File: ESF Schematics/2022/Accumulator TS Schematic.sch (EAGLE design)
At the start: 58 parts

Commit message: More schematic updates
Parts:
- removed U$10: CONNECTOR-2_HPK, HyTechSymbolsTemp:CONNECTOR-2_HPK
- added J1, J2: CONNECTOR-1_LCAX2-14F-E, HyTechSymbolsTemp:CONNECTOR-1_LCAX2-14F-E
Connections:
- net GND: now also U$11.GND
- net SHDN: now also U$11.VCC
- net TS+UNFUSED: now also J2.1; no longer U$10.1
- net TS-UNFUSED: now also J1.1; no longer U$10.2
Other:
- note added: "10 mil"
- note added: "10 mil:"
- note added: "16AWG"
- note added: "16AWG:"
- note added: "22AWG"
- note removed: "35mm^2:"
- moved on the sheet: F3

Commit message: final drafts of most schematics
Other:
- note added: "17.5mm^2:"
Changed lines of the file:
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@@
 <text x="12.7" y="53.34" size="3.048" layer="97" align="top-left">Wire Gauge Key</text>
 <text x="12.7" y="35.56" size="1.778" layer="97" align="top-left">22AWG:</text>
-<text x="12.7" y="45.72" size="1.778" layer="97" align="top-left">20mm^2</text>
+<text x="12.7" y="45.72" size="1.778" layer="97" align="top-left">17.5mm^2:</text>
 <wire x1="241.3" y1="101.6" x2="269.24" y2="101.6" width="0.1524" layer="97" style="shortdash"/>
 <wire x1="269.24" y1="101.6" x2="269.24" y2="86.36" width="0.1524" layer="97" style="shortdash"/>
@@
 <segment>
 <pinref part="U$6" gate="G$1" pin="-"/>
-<wire x1="129.54" y1="144.78" x2="134.62" y2="144.78" width="0.508" layer="91"/>
-<wire x1="134.62" y1="144.78" x2="134.62" y2="152.4" width="0.508" layer="91"/>
+<wire x1="129.54" y1="144.78" x2="134.62" y2="144.78" width="0.4445" layer="91"/>
+<wire x1="134.62" y1="144.78" x2="134.62" y2="152.4" width="0.4445" layer="91"/>
 <pinref part="U$15" gate="G$1" pin="2"/>
-<wire x1="139.7" y1="152.4" x2="134.62" y2="152.4" width="0.508" layer="91"/>
+<wire x1="139.7" y1="152.4" x2="134.62" y2="152.4" width="0.4445" layer="91"/>
 </segment>
 </net>
@@
 </segment>
 <segment>
-<wire x1="86.36" y1="154.94" x2="86.36" y2="172.72" width="0.508" layer="91"/>
+<wire x1="86.36" y1="154.94" x2="86.36" y2="172.72" width="0.4445" layer="91"/>
 <pinref part="U$3" gate="G$1" pin="+"/>
-<wire x1="86.36" y1="172.72" x2="91.44" y2="172.72" width="0.508" layer="91"/>
+<wire x1="86.36" y1="172.72" x2="91.44" y2="172.72" width="0.4445" layer="91"/>
 <label x="68.58" y="154.94" size="1.27" layer="95"/>
 <pinref part="U$16" gate="G$1" pin="1"/>
-<wire x1="78.74" y1="154.94" x2="86.36" y2="154.94" width="0.508" layer="91"/>
+<wire x1="78.74" y1="154.94" x2="86.36" y2="154.94" width="0.4445" layer="91"/>
 </segment>
 <segment>
@@
 <segment>
 <pinref part="AIR+" gate="G$1" pin="CONTACT1"/>
-<wire x1="53.34" y1="152.4" x2="48.26" y2="152.4" width="0.508" layer="91"/>
+<wire x1="53.34" y1="152.4" x2="48.26" y2="152.4" width="0.4445" layer="91"/>
 <pinref part="MAIN_FUSE" gate="G$1" pin="2"/>
 </segment>
@@
 <segment>
 <pinref part="MAIN_FUSE" gate="G$1" pin="1"/>
-<wire x1="40.64" y1="152.4" x2="38.1" y2="152.4" width="0.508" layer="91"/>
+<wire x1="40.64" y1="152.4" x2="38.1" y2="152.4" width="0.4445" layer="91"/>
 <pinref part="U$14" gate="G$1" pin="HV+IN"/>
-<wire x1="38.1" y1="152.4" x2="17.78" y2="152.4" width="0.508" layer="91"/>
+<wire x1="38.1" y1="152.4" x2="17.78" y2="152.4" width="0.4445" layer="91"/>
 <wire x1="53.34" y1="137.16" x2="38.1" y2="137.16" width="0.1524" layer="91"/>
 <wire x1="38.1" y1="137.16" x2="38.1" y2="152.4" width="0.1524" layer="91"/>
@@
 <segment>
 <pinref part="U$14" gate="G$1" pin="HV-OUT"/>
-<wire x1="35.56" y1="129.54" x2="53.34" y2="129.54" width="0.508" layer="91"/>
-<wire x1="17.78" y1="142.24" x2="35.56" y2="142.24" width="0.508" layer="91"/>
-<wire x1="35.56" y1="142.24" x2="35.56" y2="134.62" width="0.508" layer="91"/>
+<wire x1="35.56" y1="129.54" x2="53.34" y2="129.54" width="0.4445" layer="91"/>
+<wire x1="17.78" y1="142.24" x2="35.56" y2="142.24" width="0.4445" layer="91"/>
+<wire x1="35.56" y1="142.24" x2="35.56" y2="134.62" width="0.4445" layer="91"/>
 <label x="25.4" y="144.78" size="1.27" layer="95" align="top-left"/>
 <pinref part="F3" gate="G$1" pin="2"/>
-<wire x1="35.56" y1="134.62" x2="35.56" y2="129.54" width="0.508" layer="91"/>
+<wire x1="35.56" y1="134.62" x2="35.56" y2="129.54" width="0.4445" layer="91"/>
 <wire x1="33.02" y1="134.62" x2="35.56" y2="134.62" width="0.1524" layer="91"/>
 <junction x="35.56" y="134.62"/>
@@
 <segment>
 <pinref part="AIR-" gate="G$1" pin="CONTACT2"/>
-<wire x1="175.26" y1="154.94" x2="167.64" y2="154.94" width="0.508" layer="91"/>
+<wire x1="175.26" y1="154.94" x2="167.64" y2="154.94" width="0.4445" layer="91"/>
 <label x="167.64" y="154.94" size="1.27" layer="95"/>
-<wire x1="175.26" y1="129.54" x2="175.26" y2="154.94" width="0.508" layer="91"/>
+<wire x1="175.26" y1="129.54" x2="175.26" y2="154.94" width="0.4445" layer="91"/>
 <pinref part="U$14" gate="G$1" pin="HV-IN"/>
-<wire x1="83.82" y1="129.54" x2="175.26" y2="129.54" width="0.508" layer="91"/>
+<wire x1="83.82" y1="129.54" x2="175.26" y2="129.54" width="0.4445" layer="91"/>
 </segment>
 </net>
@@
 <segment>
 <pinref part="U$3" gate="G$1" pin="-"/>
-<wire x1="91.44" y1="144.78" x2="96.52" y2="144.78" width="0.508" layer="91"/>
+<wire x1="91.44" y1="144.78" x2="96.52" y2="144.78" width="0.4445" layer="91"/>
 <pinref part="U$7" gate="G$1" pin="2"/>
-<wire x1="96.52" y1="144.78" x2="96.52" y2="175.26" width="0.508" layer="91"/>
+<wire x1="96.52" y1="144.78" x2="96.52" y2="175.26" width="0.4445" layer="91"/>
 </segment>
 </net>
@@
 <segment>
 <pinref part="U$7" gate="G$1" pin="1"/>
-<wire x1="99.06" y1="175.26" x2="99.06" y2="172.72" width="0.508" layer="91"/>
+<wire x1="99.06" y1="175.26" x2="99.06" y2="172.72" width="0.4445" layer="91"/>
 <pinref part="U$4" gate="G$1" pin="+"/>
-<wire x1="99.06" y1="172.72" x2="104.14" y2="172.72" width="0.508" layer="91"/>
+<wire x1="99.06" y1="172.72" x2="104.14" y2="172.72" width="0.4445" layer="91"/>
 </segment>
 </net>
@@
 <segment>
 <pinref part="U$4" gate="G$1" pin="-"/>
-<wire x1="104.14" y1="144.78" x2="109.22" y2="144.78" width="0.508" layer="91"/>
+<wire x1="104.14" y1="144.78" x2="109.22" y2="144.78" width="0.4445" layer="91"/>
 <pinref part="U$8" gate="G$1" pin="2"/>
-<wire x1="109.22" y1="144.78" x2="109.22" y2="175.26" width="0.508" layer="91"/>
+<wire x1="109.22" y1="144.78" x2="109.22" y2="175.26" width="0.4445" layer="91"/>
 </segment>
 </net>
@@
 <segment>
 <pinref part="U$8" gate="G$1" pin="1"/>
-<wire x1="111.76" y1="175.26" x2="116.84" y2="175.26" width="0.508" layer="91"/>
-<wire x1="116.84" y1="175.26" x2="116.84" y2="172.72" width="0.508" layer="91"/>
+<wire x1="111.76" y1="175.26" x2="116.84" y2="175.26" width="0.4445" layer="91"/>
+<wire x1="116.84" y1="175.26" x2="116.84" y2="172.72" width="0.4445" layer="91"/>
 <pinref part="U$5" gate="G$1" pin="+"/>
 </segment>
@@
 <pinref part="U$5" gate="G$1" pin="-"/>
 <pinref part="U$9" gate="G$1" pin="2"/>
-<wire x1="116.84" y1="144.78" x2="121.92" y2="144.78" width="0.508" layer="91"/>
-<wire x1="121.92" y1="144.78" x2="121.92" y2="175.26" width="0.508" layer="91"/>
+<wire x1="116.84" y1="144.78" x2="121.92" y2="144.78" width="0.4445" layer="91"/>
+<wire x1="121.92" y1="144.78" x2="121.92" y2="175.26" width="0.4445" layer="91"/>
 </segment>
 </net>
@@
 <segment>
 <pinref part="U$9" gate="G$1" pin="1"/>
-<wire x1="124.46" y1="175.26" x2="129.54" y2="175.26" width="0.508" layer="91"/>
-<wire x1="129.54" y1="175.26" x2="129.54" y2="172.72" width="0.508" layer="91"/>
+<wire x1="124.46" y1="175.26" x2="129.54" y2="175.26" width="0.4445" layer="91"/>
+<wire x1="129.54" y1="175.26" x2="129.54" y2="172.72" width="0.4445" layer="91"/>
 <pinref part="U$6" gate="G$1" pin="+"/>
 </segment>
@@
 <pinref part="U$15" gate="G$1" pin="1"/>
 <pinref part="AIR-" gate="G$1" pin="CONTACT1"/>
-<wire x1="142.24" y1="152.4" x2="152.4" y2="152.4" width="0.508" layer="91"/>
+<wire x1="142.24" y1="152.4" x2="152.4" y2="152.4" width="0.4445" layer="91"/>
 </segment>
 </net>
@@
 <pinref part="AIR+" gate="G$1" pin="CONTACT2"/>
 <pinref part="U$16" gate="G$1" pin="2"/>
-<wire x1="68.58" y1="154.94" x2="76.2" y2="154.94" width="0.508" layer="91"/>
+<wire x1="68.58" y1="154.94" x2="76.2" y2="154.94" width="0.4445" layer="91"/>
 </segment>
 </net>
@@
 <net name="N$42" class="0">
 <segment>
-<wire x1="25.4" y1="45.72" x2="35.56" y2="45.72" width="0.508" layer="91"/>
-</segment>
-</net>
+<wire x1="25.4" y1="45.72" x2="35.56" y2="45.72" width="0.4445" layer="91"/>
+</segment>
+</net>

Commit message: ESF review changes
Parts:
- DISCHARGE_RES: value 10K -> 10k
- PRECHARGE_RES: value 1.5K -> 1.5k
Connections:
- removed net TS_UNFUSED: TSMP-RES.2
- new net +5V: U$11.VCC
- net SHDN: no longer U$11.VCC
- net TS-UNFUSED: now also TSMP-RES.2
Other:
- note added: "Add HVD panduits fix resistor dividers fix busbar labelling and gauges rename relay_ctrl as precharge_ok fix maintenance plug symbol fix TSMPs add isolation for DCDC prechargeOK same as relay_ctrl show all microfit connectors ring terminals between fused and unfused and pack plus"
- moved on the sheet: TSMP+, TSMP+RES, TSMP-, TSMP-RES
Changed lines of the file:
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@@
 <part name="P2" library="HyTechSupplies" deviceset="GND" device=""/>
 <part name="P3" library="HyTechSupplies" deviceset="GND" device=""/>
-<part name="PRECHARGE_RES" library="HyTechDevices" deviceset="RESISTOR_VALUE" device="" value="1.5K"/>
+<part name="PRECHARGE_RES" library="HyTechDevices" deviceset="RESISTOR_VALUE" device="" value="1.5k"/>
 <part name="P4" library="HyTechSupplies" deviceset="TS+UNFUSED" device=""/>
 <part name="TSMP-RES" library="HyTechDevices" deviceset="RESISTOR_VALUE" device="" value="10K"/>
@@
 <part name="P6" library="HyTechSupplies" deviceset="TS+UNFUSED" device=""/>
 <part name="P7" library="HyTechSupplies" deviceset="TS-UNFUSED" device=""/>
-<part name="DISCHARGE_RES" library="HyTechDevices" deviceset="RESISTOR_VALUE" device="" value="10K"/>
+<part name="DISCHARGE_RES" library="HyTechDevices" deviceset="RESISTOR_VALUE" device="" value="10k"/>
 <part name="U$14" library="HyTechSymbolsTemp" deviceset="ENERGY_METER" device=""/>
 <part name="F1" library="HyTechSymbolsTemp" deviceset="FUSE" device="" value="10A"/>
@@
 </part>
 <part name="P12" library="HyTechSupplies" deviceset="GND" device=""/>
+<part name="P13" library="HyTechSupplies" deviceset="TS+UNFUSED" device=""/>
+<part name="P14" library="HyTechSupplies" deviceset="TS-UNFUSED" device=""/>
+<part name="P15" library="HyTechSupplies" deviceset="+5V" device=""/>
 </parts>
 <sheets>
@@
 <text x="17.78" y="144.78" size="1.27" layer="97" align="top-left">20mm^2</text>
 <text x="17.78" y="154.94" size="1.27" layer="97" align="top-left">20mm^2</text>
-<text x="83.82" y="132.08" size="1.27" layer="97" align="top-left">20mm^2</text>
 <text x="147.32" y="154.94" size="1.27" layer="97" align="top-left">20mm^2</text>
 <text x="129.54" y="142.24" size="1.27" layer="97">20mm^2</text>
@@
 <text x="91.44" y="142.24" size="1.27" layer="97">20mm^2</text>
 <text x="55.88" y="111.76" size="1.27" layer="97" align="top-left">22AWG</text>
-<text x="17.78" y="119.38" size="1.27" layer="97" align="top-left">22AWG</text>
+<text x="17.78" y="81.28" size="1.27" layer="97" align="top-left">22AWG</text>
 <text x="40.64" y="139.7" size="1.27" layer="97" align="top-left">22AWG</text>
 <text x="33.02" y="162.56" size="1.27" layer="97" align="top-left">22AWG</text>
@@
 <text x="88.9" y="193.04" size="1.27" layer="97" align="top-left">22AWG</text>
 <text x="50.8" y="76.2" size="1.27" layer="97" align="top-left">16AWG</text>
+<text x="228.6" y="198.12" size="1.778" layer="88" align="top-left">Add HVD panduits
+fix resistor dividers
+fix busbar labelling and gauges
+rename relay_ctrl as precharge_ok
+fix maintenance plug symbol
+fix TSMPs
+add isolation for DCDC
+prechargeOK same as relay_ctrl
+show all microfit connectors
+ring terminals between fused and unfused and pack plus</text>
 </plain>
 <instances>
@@
 <attribute name="VALUE" x="101.6" y="109.22" size="1.27" layer="96" align="bottom-center"/>
 </instance>
-<instance part="TSMP-RES" gate="G$1" x="27.94" y="114.3" smashed="yes">
-<attribute name="NAME" x="26.67" y="115.57" size="1.27" layer="95" align="bottom-center"/>
-<attribute name="VALUE" x="26.67" y="113.03" size="1.27" layer="96" align="top-center"/>
-</instance>
-<instance part="TSMP+RES" gate="G$1" x="27.94" y="121.92" smashed="yes">
-<attribute name="NAME" x="26.67" y="123.19" size="1.27" layer="95" align="bottom-center"/>
-<attribute name="VALUE" x="26.67" y="120.65" size="1.27" layer="96" align="top-center"/>
-</instance>
-<instance part="TSMP+" gate="G$1" x="17.78" y="121.92" smashed="yes">
-<attribute name="NAME" x="15.24" y="123.698" size="1.27" layer="95"/>
-</instance>
-<instance part="TSMP-" gate="G$1" x="17.78" y="114.3" smashed="yes">
-<attribute name="NAME" x="15.24" y="116.078" size="1.27" layer="95"/>
+<instance part="TSMP-RES" gate="G$1" x="27.94" y="76.2" smashed="yes">
+<attribute name="NAME" x="26.67" y="77.47" size="1.27" layer="95" align="bottom-center"/>
+<attribute name="VALUE" x="26.67" y="74.93" size="1.27" layer="96" align="top-center"/>
+</instance>
+<instance part="TSMP+RES" gate="G$1" x="27.94" y="83.82" smashed="yes">
+<attribute name="NAME" x="26.67" y="85.09" size="1.27" layer="95" align="bottom-center"/>
+<attribute name="VALUE" x="26.67" y="82.55" size="1.27" layer="96" align="top-center"/>
+</instance>
+<instance part="TSMP+" gate="G$1" x="17.78" y="83.82" smashed="yes">
+<attribute name="NAME" x="15.24" y="85.598" size="1.27" layer="95"/>
+</instance>
+<instance part="TSMP-" gate="G$1" x="17.78" y="76.2" smashed="yes">
+<attribute name="NAME" x="15.24" y="77.978" size="1.27" layer="95"/>
 </instance>
 <instance part="DISCHARGE" gate="G$1" x="139.7" y="116.84" smashed="yes">
@@
 <attribute name="VALUE" x="71.12" y="181.61" size="1.27" layer="96" align="top-center"/>
 </instance>
+<instance part="P13" gate="G$1" x="33.02" y="86.36" smashed="yes">
+<attribute name="VALUE" x="33.02" y="91.44" size="1.27" layer="96" align="bottom-center"/>
+</instance>
+<instance part="P14" gate="G$1" x="33.02" y="73.66" smashed="yes">
+<attribute name="VALUE" x="33.02" y="71.12" size="1.27" layer="96" align="top-center"/>
+</instance>
+<instance part="P15" gate="1" x="71.12" y="190.5" smashed="yes">
+<attribute name="VALUE" x="71.12" y="193.04" size="1.27" layer="96" align="bottom-center"/>
+</instance>
 </instances>
 <busses>
@@
 <wire x1="132.08" y1="195.58" x2="134.62" y2="195.58" width="0.1524" layer="91"/>
 <label x="134.62" y="195.58" size="1.27" layer="95" xref="yes"/>
-</segment>
-<segment>
-<pinref part="U$11" gate="G$1" pin="VCC"/>
-<wire x1="68.58" y1="187.96" x2="71.12" y2="187.96" width="0.1524" layer="91"/>
-<label x="71.12" y="187.96" size="1.27" layer="95" xref="yes"/>
 </segment>
 </net>
@@
 <segment>
 <pinref part="TSMP+RES" gate="G$1" pin="2"/>
-<wire x1="30.48" y1="121.92" x2="33.02" y2="121.92" width="0.1524" layer="91"/>
-<label x="33.02" y="121.92" size="1.27" layer="95" xref="yes"/>
+<wire x1="30.48" y1="83.82" x2="33.02" y2="83.82" width="0.1524" layer="91"/>
+<pinref part="P13" gate="G$1" pin="TS+UNFUSED"/>
 </segment>
 <segment>
@@
 <segment>
 <pinref part="TSMP+RES" gate="G$1" pin="1"/>
-<wire x1="22.86" y1="121.92" x2="20.32" y2="121.92" width="0.1524" layer="91"/>
+<wire x1="22.86" y1="83.82" x2="20.32" y2="83.82" width="0.1524" layer="91"/>
 <pinref part="TSMP+" gate="G$1" pin="P$1"/>
 </segment>
@@
 <segment>
 <pinref part="TSMP-RES" gate="G$1" pin="1"/>
-<wire x1="22.86" y1="114.3" x2="20.32" y2="114.3" width="0.1524" layer="91"/>
+<wire x1="22.86" y1="76.2" x2="20.32" y2="76.2" width="0.1524" layer="91"/>
 <pinref part="TSMP-" gate="G$1" pin="P$1"/>
-</segment>
-</net>
-<net name="TS_UNFUSED" class="0">
-<segment>
-<pinref part="TSMP-RES" gate="G$1" pin="2"/>
-<wire x1="30.48" y1="114.3" x2="33.02" y2="114.3" width="0.1524" layer="91"/>
-<label x="33.02" y="114.3" size="1.27" layer="95" xref="yes"/>
 </segment>
 </net>
@@
 <junction x="200.66" y="73.66"/>
 <pinref part="U$28" gate="G$1" pin="TS-UNFUSED"/>
+</segment>
+<segment>
+<pinref part="TSMP-RES" gate="G$1" pin="2"/>
+<wire x1="30.48" y1="76.2" x2="33.02" y2="76.2" width="0.1524" layer="91"/>
+<pinref part="P14" gate="G$1" pin="TS-UNFUSED"/>
 </segment>
 </net>
@@
 </segment>
 </net>
+<net name="+5V" class="0">
+<segment>
+<pinref part="U$11" gate="G$1" pin="VCC"/>
+<wire x1="68.58" y1="187.96" x2="71.12" y2="187.96" width="0.1524" layer="91"/>
+<pinref part="P15" gate="1" pin="+5V"/>
+</segment>
+</net>

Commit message: more updates
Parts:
- removed TSMP+, TSMP-: TEST_POINT, HyTechDevices:TEST_POINT
- added J3, J4: CONNECTOR-1_LCAX2-14F-E, HyTechSymbolsTemp:CONNECTOR-1_LCAX2-14F-E
- added RV24, RV25: 365k, HyTechDevices:RESISTOR_VALUE
- added U$31, U$32, U$33, U$34, U$35: MAINTENANCE_PLUG_104742-2, HyTechSymbolsTemp:MAINTENANCE_PLUG_104742-2
- added U$36, U$37, U$38: RING_TERMINAL_19054-0042, HyTechSymbolsTemp:RING_TERMINAL_19054-0042
- U$15, U$16, U$7, U$8, U$9: value CONNECTOR-2_104742-2 -> MAINTENANCE_PLUG_104742-2; device HyTechSymbolsTemp:CONNECTOR-2_104742-2 -> HyTechSymbolsTemp:MAINTENANCE_PLUG_104742-2
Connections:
- removed net N$10: TSMP-.P$1, TSMP-RES.1
- removed net N$9: TSMP+.P$1, TSMP+RES.1
- removed net RELAY_CTRL: AIR+.COIL-, U$11.RELAY_CTRL, U$30.RELAY_CTRL
- new net N$45: J3.1, U$14.HV-IN
- new net N$47: AIR-.CONTACT2, J4.1
- new net N$48: RV24.1, RV5.2, RV6.2, U$27.IN
- new net N$49: AIR-.CONTACT1, U$35.1
- new net N$50: F3.2, U$36.P$1
- new net N$51: F2.2, U$37.P$1
- net N$1: now also U$7.1; no longer U$7.2
- net N$14: now also RV24.2, RV4.1; no longer AIR-.CONTACT2, U$14.HV-IN
- net N$16: now also U$34.1, U$6.-; no longer AIR-.CONTACT1, U$15.1
- net N$17: now also U$32.1; no longer U$16.2
- net N$2: now also U$15.1; no longer U$8.2
- net N$21: now also U$15.P$1, U$9.P$1; no longer RV4.1, RV5.2, RV6.2, U$27.IN
- net N$22: now also RV5.1, RV7.2
- net N$23: now also U$16.P$1, U$31.P$1; no longer RV5.1, RV7.2
- net N$24: now also RV14.1, RV25.2; no longer RV7.1, RV9.2
- net N$25: now also RV7.1, RV9.2
- net N$29: now also RV25.1; no longer RV14.1
- net N$3: now also U$16.1; no longer U$9.2
- net N$30: now also U$32.P$1, U$33.P$1, U$38.P$1; no longer RV16.1, RV18.2
- net N$31: now also RV16.1, RV18.2
- net N$32: now also RV18.1, RV20.2
- net N$33: now also U$34.P$1, U$35.P$1; no longer RV18.1, RV20.2
- net N$4: now also U$8.1; no longer U$7.1
- net N$5: now also U$9.1; no longer U$8.1
- net N$6: now also U$31.1; no longer U$9.1
- net N$7: now also U$7.P$1, U$8.P$1; no longer U$15.2, U$6.-
- net PACK+: now also U$33.1, U$38.P$2; no longer U$16.1
- net PRECHARGE_OK: now also AIR+.COIL-, U$11.PRECHARGE_OK
- net TS+UNFUSED: now also U$37.P$2; no longer F2.2
- net TS-UNFUSED: now also U$36.P$2; no longer F3.2
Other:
- note added: "(Busbar)"
- note added: "17.5mm^2"
- note added: "Add HVD panduits-done fix resistor dividers-done fix busbar labelling and gauges-done rename relay_ctrl as precharge_ok-done fix maintenance plug symbol-done fix TSMPs add isolation for DCDC-done prechargeOK same as relay_ctrl-done show all microfit connectors ring terminals between fused and unfused and pack plus-done"
- note removed: "20mm^2"
- note removed: "Add HVD panduits fix resistor dividers fix busbar labelling and gauges rename relay_ctrl as precharge_ok fix maintenance plug symbol fix TSMPs add isolation for DCDC prechargeOK same as relay_ctrl show all microfit connectors ring terminals between fused and unfused and pack plus"
- moved on the sheet: AIR-, F1, F2, F3, RV10, RV11, RV12, RV13, RV14, RV5, RV6, RV7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

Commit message: fixups after the ESF review
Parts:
- added J5, J7: CONNECTOR-1_, HyTechSymbolsTemp:CONNECTOR-1_
- added J6, J8: CONNECTOR-5_MICROFIT, HyTechSymbolsTemp:CONNECTOR-5_MICROFIT
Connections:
- net N$34 renamed OUTNB
- net N$35 renamed OUTPB
- net N$36 renamed OUTNA
- net N$37 renamed OUTPA
- new net TSMP+: J5.1, J6.3, TSMP+RES.1
- new net TSMP-: J7.1, J8.4, TSMP-RES.1
- net PACK+: now also J6.5
- net TS+: now also J6.4
- net TS+UNFUSED: now also J6.1, J6.2
- net TS-UNFUSED: now also J8.1, J8.2, J8.5
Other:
- note added: "(>= 20 mil)"
- note added: "Accumulator Internal TS Connectors"
- note added: "Add HVD panduits-done fix resistor dividers-done fix busbar labelling and gauges-done rename relay_ctrl as precharge_ok-done fix maintenance plug symbol-done fix TSMPs add isolation for DCDC-done prechargeOK same as relay_ctrl-done show all microfit connectors-done ring terminals between fused and unfused and pack plus-done"
- note added: "PCB Trace"
- note added: "PCB Trace:"
- note removed: "10 mil"
- note removed: "10 mil:"
- note removed: "Add HVD panduits-done fix resistor dividers-done fix busbar labelling and gauges-done rename relay_ctrl as precharge_ok-done fix maintenance plug symbol-done fix TSMPs add isolation for DCDC-done prechargeOK same as relay_ctrl-done show all microfit connectors ring terminals between fused and unfused and pack plus-done"
- moved on the sheet: TSMP+RES, TSMP-RES

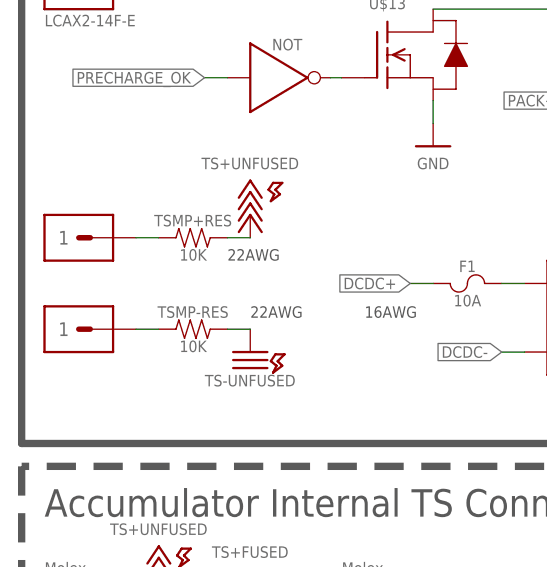
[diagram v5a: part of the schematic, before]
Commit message: final fixes from ESF review
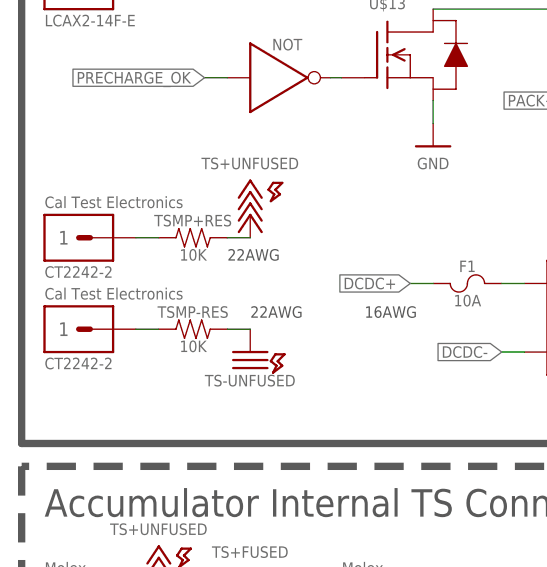
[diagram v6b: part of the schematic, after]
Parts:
- J5, J7: value CONNECTOR-1_ -> CONNECTOR-1_CT2242-2; device HyTechSymbolsTemp:CONNECTOR-1_ -> HyTechSymbolsTemp:CONNECTOR-1_CT2242-2
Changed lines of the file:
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@@
 <part name="P19" library="HyTechSupplies" deviceset="TS-UNFUSED" device=""/>
 <part name="U$40" library="HyTechSupplies" deviceset="TS-FUSED" device=""/>
-<part name="J5" library="HyTechSymbolsTemp" deviceset="CONNECTOR-1_*" device=""/>
-<part name="J7" library="HyTechSymbolsTemp" deviceset="CONNECTOR-1_*" device=""/>
+<part name="J5" library="HyTechSymbolsTemp" deviceset="CONNECTOR-1_*" device="" technology="CT2242-2" value="CONNECTOR-1_CT2242-2"/>
+<part name="J7" library="HyTechSymbolsTemp" deviceset="CONNECTOR-1_*" device="" technology="CT2242-2" value="CONNECTOR-1_CT2242-2"/>
 </parts>
 <sheets>
